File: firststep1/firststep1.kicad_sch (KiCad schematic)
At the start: 0 parts

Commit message: many changes
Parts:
- added BZ1: Buzzer, Buzzer_Beeper:Buzzer_12x9.5RM7.6, symbol Device:Buzzer
- added C6, C8: 1u, Capacitor_THT:C_Disc_D3.0mm_W2.0mm_P2.50mm, symbol Device:C
- added C7: 3,3u, Capacitor_THT:C_Disc_D3.0mm_W2.0mm_P2.50mm, symbol Device:C
- added C9: 0,1u, Capacitor_THT:C_Disc_D3.0mm_W2.0mm_P2.50mm, symbol Device:C
- added C?: 4,7u, Capacitor_THT:C_Disc_D3.0mm_W2.0mm_P2.50mm, symbol Device:C
- added D2: SP0502BAHT, Package_TO_SOT_SMD:SOT-23, symbol Power_Protection:SP0502BAHT
- added J1: Conn_01x02, Connector_Wago:Wago_734-162_1x02_P3.50mm_Horizontal, symbol Connector_Generic:Conn_01x02
- added L1: 100uH, symbol Device:L
- added LA1: BackLamp, symbol Device:Lamp
- added R16, R17: 3,3, Resistor_THT:R_Axial_DIN0204_L3.6mm_D1.6mm_P7.62mm_Horizontal, symbol Device:R
- added R2 (x8): 330, R_Axial_DIN0207_L6.3mm_D2.5mm_P7.62mm_Horizontal, symbol Device:R
- added R9: 470, Resistor_THT:R_Axial_DIN0207_L6.3mm_D2.5mm_P7.62mm_Horizontal, symbol Device:R
- added SW1: RELAY_SW, symbol Switch:SW_SPST
- added U4: ATmega48V-10A, Package_QFP:TQFP-32_7x7mm_P0.8mm, symbol MCU_Microchip_ATmega:ATmega48V-10A
- added U5: MIC4428, Package_DIP:DIP-8_W7.62mm_Socket, symbol Driver_FET:MIC4428
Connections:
- new net: C6.1, R2.1, R2.2, U4.22 (ADC7)
- new net: R17.1, U5.5 (OUT_B)
- new net: C7.1, R2.1, U5.6 (V+)
- new net: R16.1, U5.7 (~{OUT_A})
- new net: BZ1.1 (-), R9.1
- new net: R9.2, U4.1 (PD3)
- new net +12V: LA1.2 (+), R2.2, R2.2, SW1.2 (B)
- new net +5V: L1.1
- new net 5VDC: C?.1, L1.2, U4.18 (AVCC)
- new net ADC6: U4.19 (ADC6)
- new net FET_GATE: R16.2
- new net GND: BZ1.2 (+), C6.2, C7.2, C8.2, C9.1, C?.2, D2.3 (A), J1.1 (Pin_1), LA1.1 (-), R2.1, R2.1, R2.1, U4.21 (GND), U4.3 (GND), U4.5 (GND), U5.3 (GND)
- new net PB1: R2.2, U4.13 (PB1), U5.2 (IN_A), U5.4 (IN_B)
- new net PC6: C9.2, R2.1, U4.29 (~{RESET}/PC6)
- new net PD4: D2.2 (K), J1.2 (Pin_2), R2.1, U4.2 (PD4)
- new net PD6: R2.2, U4.10 (PD6)
- new net RELAY_PWR: R2.1, R2.2, SW1.1 (A)
- new net VCC: C8.1, R2.2, R2.2, U4.4 (VCC), U4.6 (VCC)
- no-connect marks 0 -> 15
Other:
- added sheet driver (driver.kicad_sch)

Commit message: minor
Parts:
- gave numbers to parts that had none: 1
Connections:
- no-connect marks 15 -> 28
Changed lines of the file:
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@@
   (junction (at 185.166 78.74) (diameter 0) (color 0 0 0 0)
   )
+  (junction (at 27.94 23.876) (diameter 0) (color 0 0 0 0)
+  )
   (junction (at 31.496 83.566) (diameter 0) (color 0 0 0 0)
   )
@@
   (junction (at 217.932 94.234) (diameter 0) (color 0 0 0 0)
   )
+  (junction (at 185.166 45.72) (diameter 0) (color 0 0 0 0)
+  )
   (junction (at 55.626 83.566) (diameter 0) (color 0 0 0 0)
   )
+  (junction (at 233.426 58.674) (diameter 0) (color 0 0 0 0)
+  )
   (junction (at 77.978 39.878) (diameter 0) (color 0 0 0 0)
+  )
+  (junction (at 75.438 129.286) (diameter 0) (color 0 0 0 0)
   )
   (junction (at 55.626 100.076) (diameter 0) (color 0 0 0 0)
@@
   (no_connect (at 90.678 114.554))
   (no_connect (at 90.678 86.614))
+  (no_connect (at 90.678 101.854))
+  (no_connect (at 90.678 106.934))
   (no_connect (at 90.678 58.674))
+  (no_connect (at 92.456 68.834))
+  (no_connect (at 90.678 104.394))
   (no_connect (at 90.678 73.914))
   (no_connect (at 90.678 63.754))
+  (no_connect (at 90.678 68.834))
   (no_connect (at 90.678 76.454))
+  (no_connect (at 90.678 66.294))
   (no_connect (at 200.66 121.92))
   (no_connect (at 90.678 94.234))
+  (no_connect (at 90.678 71.374))
+  (no_connect (at 92.456 104.394))
+  (no_connect (at 92.456 71.374))
+  (no_connect (at 92.456 101.854))
   (no_connect (at 90.678 119.634))
+  (no_connect (at 92.456 66.294))
+  (no_connect (at 35.052 170.942))
   (no_connect (at 90.678 91.694))
+  (no_connect (at 92.456 106.934))
   (wire (pts (xy 185.166 88.138) (xy 185.166 94.234))
     (stroke (width 0) (type default) (color 0 0 0 0))
@@
     (pin "1")
     (pin "2")
+  )
+  (symbol (lib_id "power:PWR_FLAG") (at 75.438 129.286 180) (unit 1)
+    (in_bom yes) (on_board yes) (fields_autoplaced)
+    (property "Reference" "#FLG0101" (id 0) (at 75.438 131.191 0)
+      (effects (font (size 1.27 1.27)) hide)
+    )
+    (property "Value" "PWR_FLAG" (id 1) (at 75.438 133.858 0))
+    (property "Footprint" "" (id 2) (at 75.438 129.286 0)
+      (effects (font (size 1.27 1.27)) hide)
+    )
+    (property "Datasheet" "~" (id 3) (at 75.438 129.286 0)
+      (effects (font (size 1.27 1.27)) hide)
+    )
+    (pin "1")
   )
   (symbol (lib_id "Device:R") (at 40.386 83.566 270) (unit 1)
@@
   (symbol (lib_id "Device:C") (at 88.9 39.878 90) (unit 1)
     (in_bom yes) (on_board yes) (fields_autoplaced)
-    (property "Reference" "C?" (id 0) (at 88.9 32.004 90))
+    (property "Reference" "C10" (id 0) (at 88.9 32.004 90))
     (property "Value" "4,7u" (id 1) (at 88.9 34.544 90))
     (property "Footprint" "Capacitor_THT:C_Disc_D3.0mm_W2.0mm_P2.50mm" (id 2) (at 92.71 38.9128 0)
@@
     (pin "1")
     (pin "2")
+  )
+  (symbol (lib_id "power:PWR_FLAG") (at 27.94 23.876 90) (unit 1)
+    (in_bom yes) (on_board yes) (fields_autoplaced)
+    (property "Reference" "#FLG0104" (id 0) (at 26.035 23.876 0)
+      (effects (font (size 1.27 1.27)) hide)
+    )
+    (property "Value" "PWR_FLAG" (id 1) (at 26.67 20.32 90))
+    (property "Footprint" "" (id 2) (at 27.94 23.876 0)
+      (effects (font (size 1.27 1.27)) hide)
+    )
+    (property "Datasheet" "~" (id 3) (at 27.94 23.876 0)
+      (effects (font (size 1.27 1.27)) hide)
+    )
+    (pin "1")
   )
   (symbol (lib_id "power:GND") (at 185.166 99.06 0) (unit 1)
@@
     (pin "1")
   )
+  (symbol (lib_id "power:PWR_FLAG") (at 233.426 58.674 270) (unit 1)
+    (in_bom yes) (on_board yes) (fields_autoplaced)
+    (property "Reference" "#FLG?" (id 0) (at 235.331 58.674 0)
+      (effects (font (size 1.27 1.27)) hide)
+    )
+    (property "Value" "PWR_FLAG" (id 1) (at 237.744 58.6739 90)
+      (effects (font (size 1.27 1.27)) (justify left))
+    )
+    (property "Footprint" "" (id 2) (at 233.426 58.674 0)
+      (effects (font (size 1.27 1.27)) hide)
+    )
+    (property "Datasheet" "~" (id 3) (at 233.426 58.674 0)
+      (effects (font (size 1.27 1.27)) hide)
+    )
+    (pin "1")
+  )
   (symbol (lib_id "Device:Lamp") (at 31.496 92.202 0) (unit 1)
     (in_bom yes) (on_board yes) (fields_autoplaced)
@@
   (symbol (lib_id "power:GND") (at 98.806 39.878 90) (unit 1)
     (in_bom yes) (on_board yes) (fields_autoplaced)
-    (property "Reference" "#PWR?" (id 0) (at 105.156 39.878 0)
+    (property "Reference" "#PWR03" (id 0) (at 105.156 39.878 0)
       (effects (font (size 1.27 1.27)) hide)
     )
@@
     (pin "2")
   )
+  (symbol (lib_id "power:PWR_FLAG") (at 75.438 47.752 0) (unit 1)
+    (in_bom yes) (on_board yes) (fields_autoplaced)
+    (property "Reference" "#FLG0103" (id 0) (at 75.438 45.847 0)
+      (effects (font (size 1.27 1.27)) hide)
+    )
+    (property "Value" "PWR_FLAG" (id 1) (at 77.724 46.4819 0)
+      (effects (font (size 1.27 1.27)) (justify left))
+    )
+    (property "Footprint" "" (id 2) (at 75.438 47.752 0)
+      (effects (font (size 1.27 1.27)) hide)
+    )
+    (property "Datasheet" "~" (id 3) (at 75.438 47.752 0)
+      (effects (font (size 1.27 1.27)) hide)
+    )
+    (pin "1")
+  )
   (symbol (lib_id "Device:Buzzer") (at 120.396 106.934 90) (unit 1)
     (in_bom yes) (on_board yes) (fields_autoplaced)
@@
     (pin "1")
     (pin "2")
+  )
+  (symbol (lib_id "power:PWR_FLAG") (at 185.166 45.72 90) (unit 1)
+    (in_bom yes) (on_board yes) (fields_autoplaced)
+    (property "Reference" "#FLG0102" (id 0) (at 183.261 45.72 0)
+      (effects (font (size 1.27 1.27)) hide)
+    )
+    (property "Value" "PWR_FLAG" (id 1) (at 183.896 42.164 90))
+    (property "Footprint" "" (id 2) (at 185.166 45.72 0)
+      (effects (font (size 1.27 1.27)) hide)
+    )
+    (property "Datasheet" "~" (id 3) (at 185.166 45.72 0)
+      (effects (font (size 1.27 1.27)) hide)
+    )
+    (pin "1")
   )
   (symbol (lib_id "power:GND") (at 203.2 134.62 0) (unit 1)
@@
       (reference "#FLG01") (unit 1) (value "PWR_FLAG") (footprint "")
     )
-    (path "/bbdf291e-1bd7-4944-8125-7f1ab6a05193/bf02bbdf-17e0-4435-898d-55b8c6f36567"
-      (reference "#FLG02") (unit 1) (value "PWR_FLAG") (footprint "")
+    (path "/0e380b83-f16f-45bd-b0c0-82a9aa4ca9e4"
+      (reference "#FLG0101") (unit 1) (value "PWR_FLAG") (footprint "")
+    )
+    (path "/ec1ac5b9-e966-4cca-927b-517ed8b72588"
+      (reference "#FLG0102") (unit 1) (value "PWR_FLAG") (footprint "")
+    )
+    (path "/c6c55bd9-c221-4594-b99f-2827103a4cd3"
+      (reference "#FLG0103") (unit 1) (value "PWR_FLAG") (footprint "")
+    )
+    (path "/48628146-1fc7-45d3-a7ab-f6fd595006d9"
+      (reference "#FLG0104") (unit 1) (value "PWR_FLAG") (footprint "")
+    )
+    (path "/a69cc898-cdd0-4b5a-b0cf-1ee8e3d30ca8"
+      (reference "#FLG?") (unit 1) (value "PWR_FLAG") (footprint "")
     )
     (path "/a21b11a8-27ad-47d8-8f04-8aef26576528"
@@
       (reference "#PWR02") (unit 1) (value "GND") (footprint "")
     )
+    (path "/bafb434e-a244-4dd1-bbbf-9857e55e91de"
+      (reference "#PWR03") (unit 1) (value "GND") (footprint "")
+    )
     (path "/6400ff27-d98a-48a5-8820-860faab6722a"
       (reference "#PWR05") (unit 1) (value "+12V") (footprint "")
@@
       (reference "#PWR010") (unit 1) (value "GND") (footprint "")
     )
-    (path "/bafb434e-a244-4dd1-bbbf-9857e55e91de"
-      (reference "#PWR?") (unit 1) (value "GND") (footprint "")
-    )
     (path "/d64696ea-ef07-4073-a07b-172d55c42cc2"
       (reference "BZ1") (unit 1) (value "Buzzer") (footprint "Buzzer_Beeper:Buzzer_12x9.5RM7.6")
@@
     )
     (path "/47d45b6f-f299-4e9b-80d5-bb5f7aa1cd8d"
-      (reference "C?") (unit 1) (value "4,7u") (footprint "Capacitor_THT:C_Disc_D3.0mm_W2.0mm_P2.50mm")
+      (reference "C10") (unit 1) (value "4,7u") (footprint "Capacitor_THT:C_Disc_D3.0mm_W2.0mm_P2.50mm")
     )
     (path "/bbdf291e-1bd7-4944-8125-7f1ab6a05193/85787a8f-0c3a-485b-9ce7-761a86dacadf"
@@
     )
     (path "/4a7673fc-4a97-4efb-9d89-a65949a7a152/e396bf58-8af3-4762-8218-ea13a37d7164"
-      (reference "K?") (unit 1) (value "G5LE-1") (footprint "Relay_THT:Relay_SPDT_Omron-G5LE-1")
+      (reference "K1") (unit 1) (value "G5LE-1") (footprint "Relay_THT:Relay_SPDT_Omron-G5LE-1")
     )
     (path "/33b7105a-6c60-4d8c-a480-4ad8f11d5220"

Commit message: firststep2
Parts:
- removed C6: 1u, Capacitor_THT:C_Disc_D3.0mm_W2.0mm_P2.50mm, symbol Device:C
- removed C7: 3,3u, Capacitor_THT:C_Disc_D3.0mm_W2.0mm_P2.50mm, symbol Device:C
- removed LA1: BackLamp, symbol Device:Lamp
- removed R16, R17: 3,3, Resistor_THT:R_Axial_DIN0204_L3.6mm_D1.6mm_P7.62mm_Horizontal, symbol Device:R
- removed R2 (x6): 330, R_Axial_DIN0207_L6.3mm_D2.5mm_P7.62mm_Horizontal, symbol Device:R
- removed SW1: RELAY_SW, symbol Switch:SW_SPST
- removed U5: MIC4428, Package_DIP:DIP-8_W7.62mm_Socket, symbol Driver_FET:MIC4428
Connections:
- net GND: no longer U4.21 (GND), U4.3 (GND), U4.5 (GND)
- net at U4.1 (PD3): no longer R9.2
- new net: U4.21 (GND), U4.3 (GND), U4.5 (GND)
- new net PD3: R9.2
- no-connect marks 28 -> 27
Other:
- note added: "D3"
- note added: "D4"
- note added: "RESET"
- moved on the sheet: BZ1, R9

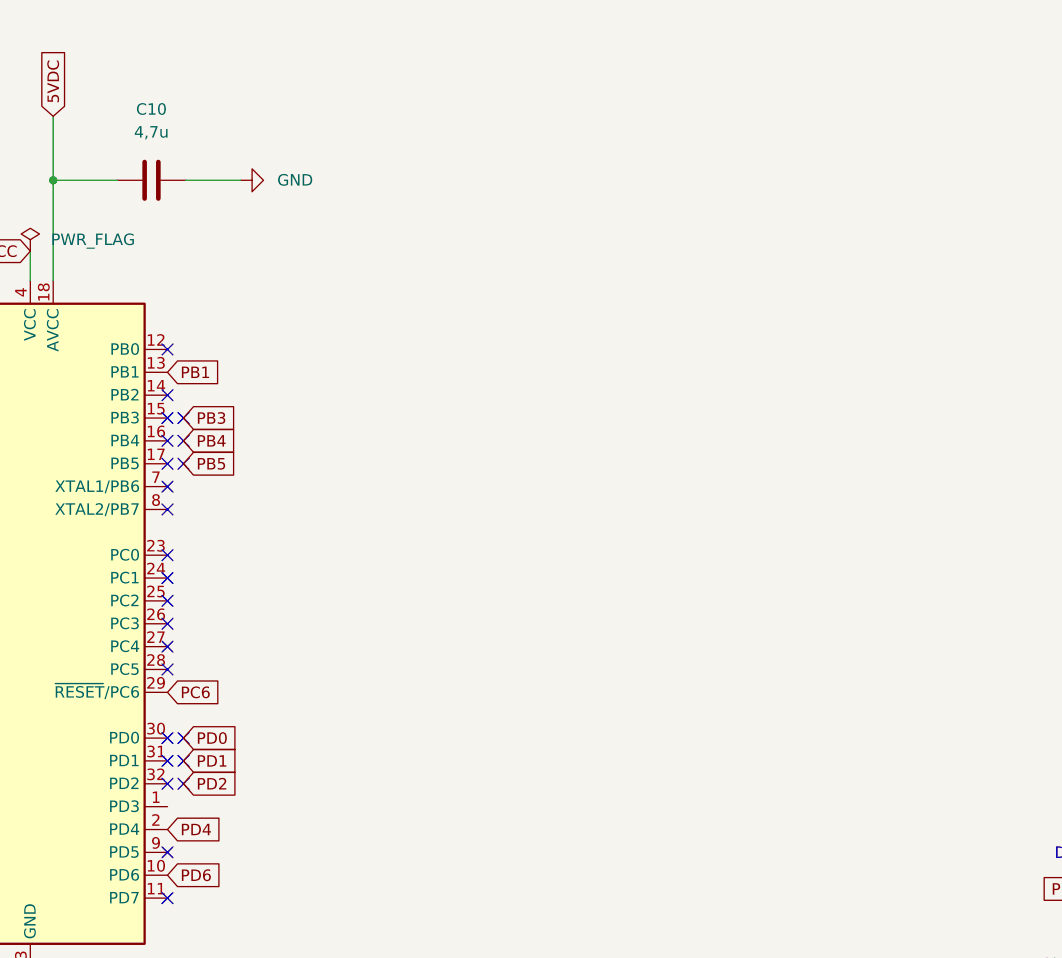
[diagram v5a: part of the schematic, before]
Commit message: add inverter
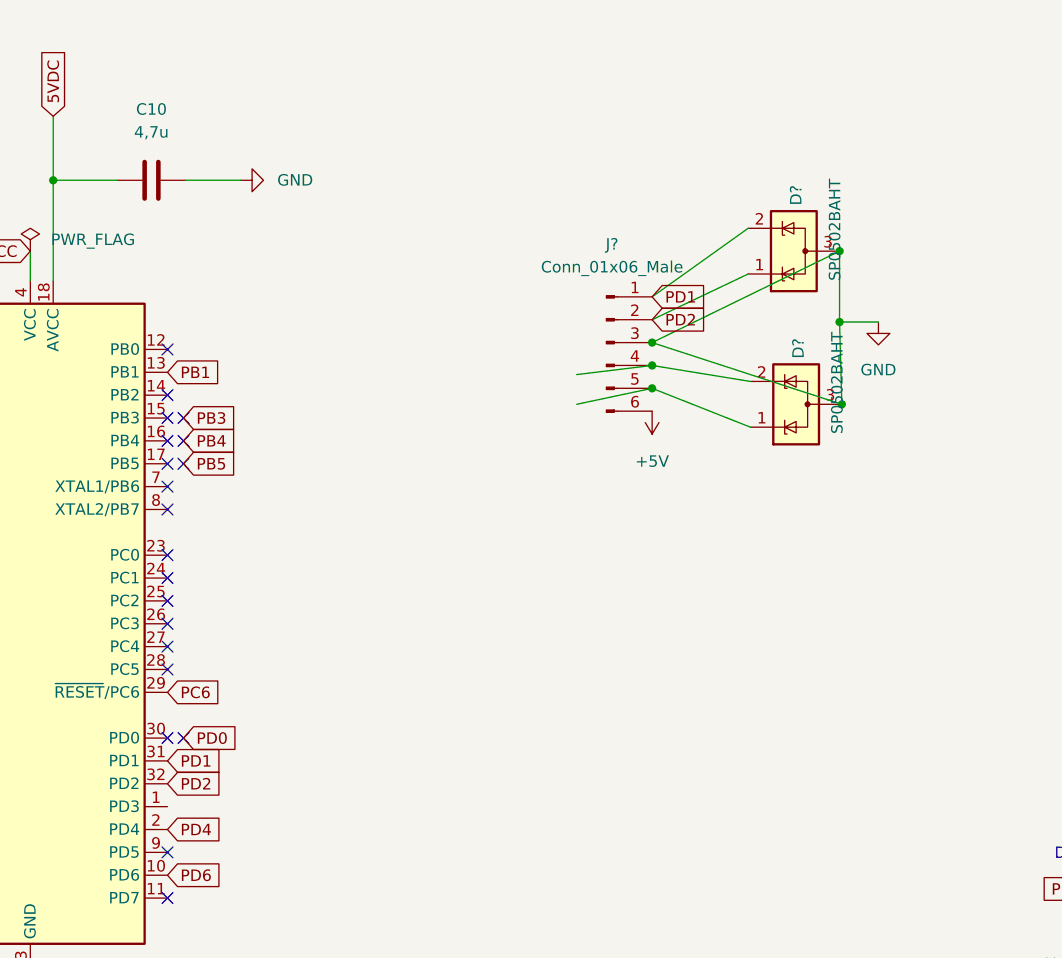
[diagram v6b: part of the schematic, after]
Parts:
- added D? (x2): SP0502BAHT, Package_TO_SOT_SMD:SOT-23, symbol Power_Protection:SP0502BAHT
- added J?: Conn_01x06_Male, symbol Connector:Conn_01x06_Male
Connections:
- net +5V: now also J?.6 (Pin_6)
- net GND: now also D?.3 (A), D?.3 (A), J?.3 (Pin_3)
- net PD1: now also U4.31 (PD1), D?.2 (K), J?.1 (Pin_1)
- net PD2: now also U4.32 (PD2), D?.1 (K), J?.2 (Pin_2)
- new net: D?.2 (K), J?.4 (Pin_4)
- new net: D?.1 (K), J?.5 (Pin_5)
- no-connect marks 27 -> 23
